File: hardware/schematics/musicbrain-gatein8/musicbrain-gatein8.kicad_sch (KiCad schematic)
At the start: 32 parts, among them J1 BUS, J2 GATES IN, U1 74HC165, U2 74LVC1G125

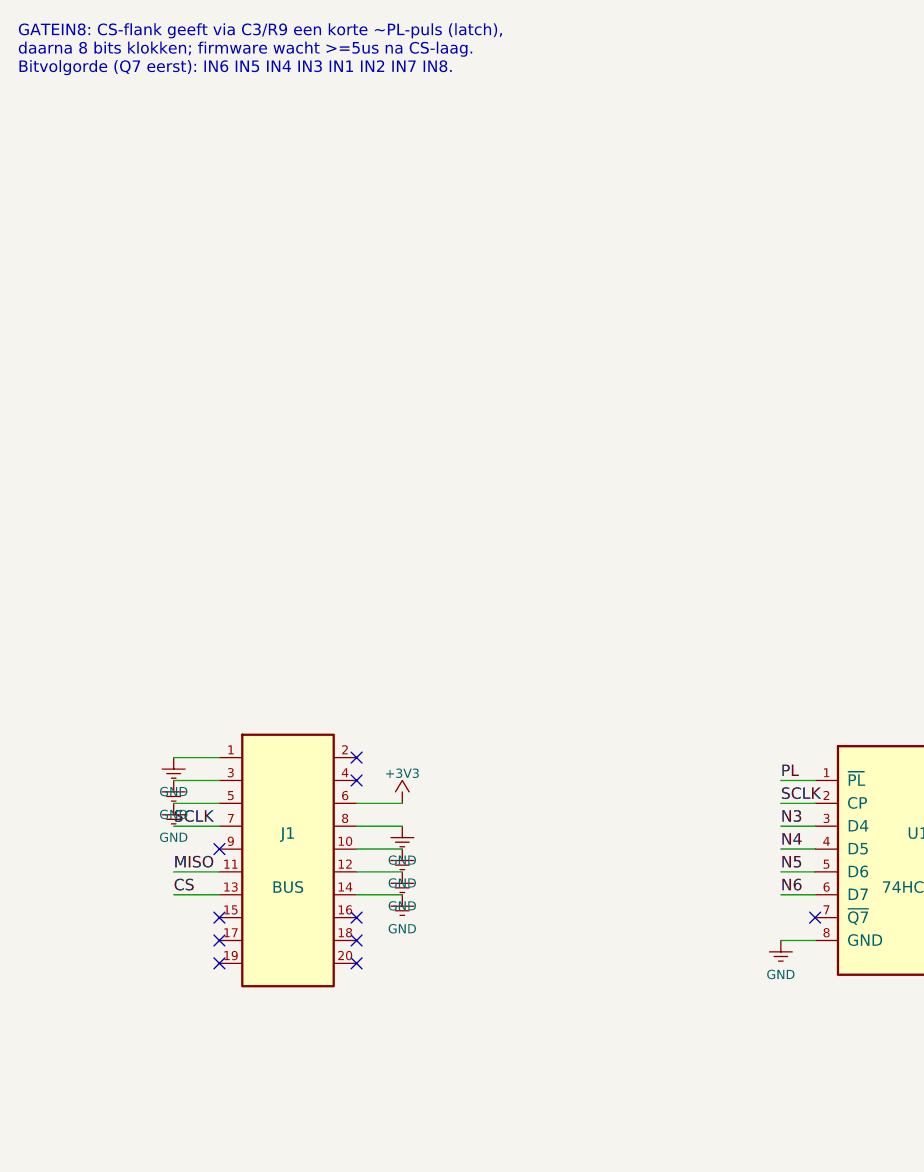
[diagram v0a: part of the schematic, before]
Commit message: gatein8 gen 2: 80x45, slot 2x12, freerouting
- kaart 40x80 -> 80x45 (bus.KAART_B x bus.H); J1 2x10 -> 2x12 via bus.j1_map
- J2 1x10 gecentreerd op het kaarthart, paneelinzet 4,04
- kanaal-conditionering (100k/100k/BAT54S) in kolommen onder de J2-pinnen;
  D_OF_IN-mapping ongewijzigd (firmware-contract)
- handroutes vervangen door freerouting-SES + gnd_stitch.json
- ERC 0, netcheck OK, DRC 0/0

Co-Authored-By: Claude Fable 5 <noreply@anthropic.com>
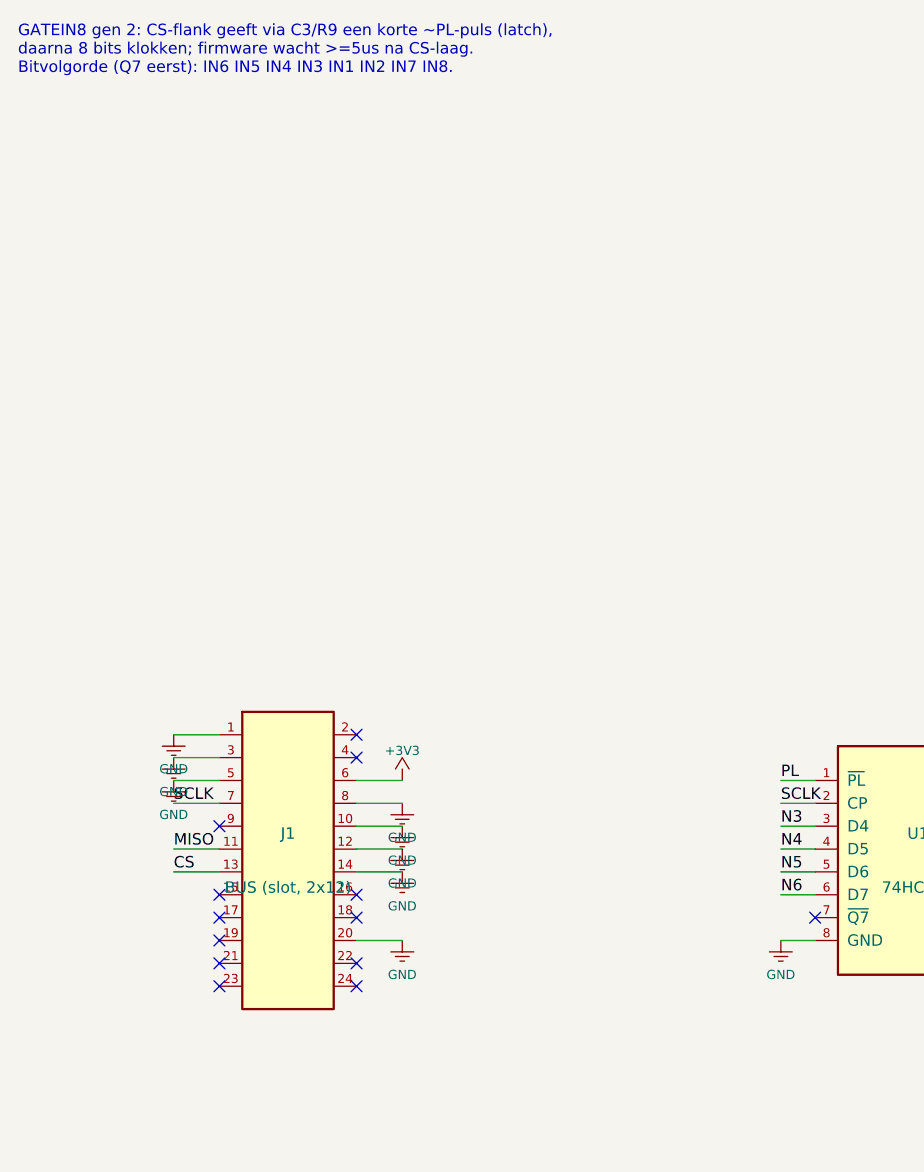
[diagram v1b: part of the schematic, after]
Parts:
- removed C1: 100n, Capacitor_SMD:C_0805_2012Metric, symbol Device:C
- removed R1, R2, R3, R4, R5, R6, R7, R8: 100k, Resistor_SMD:R_0805_2012Metric, symbol Device:R
- removed R9: 10k, Resistor_SMD:R_0805_2012Metric, symbol Device:R
- added C2: 10u, Capacitor_SMD:CP_Elec_4x5.3, symbol Device:C_Polarized
- added C3: 220p, Capacitor_SMD:C_0805_2012Metric, symbol Device:C
- added D1, D2, D3, D4, D5, D6, D7, D8: BAT54S, Package_TO_SOT_SMD:SOT-23, symbol Custom:BAT54S
- C1: renamed from C2; value 10u -> 100n; footprint Capacitor_SMD:CP_Elec_4x5.3 -> Capacitor_SMD:C_0805_2012Metric; symbol Device:C_Polarized -> Device:C
- J1: value BUS -> BUS (slot, 2x12); footprint Connector_PinHeader_2.54mm:PinHeader_2x10_P2.54mm_Horizontal -> Connector_PinHeader_2.54mm:PinHeader_2x12_P2.54mm_Horizontal; symbol Custom:Conn_02x10 -> Custom:Conn_02x12
- R11: renamed from D1; value BAT54S -> 100k; footprint Package_TO_SOT_SMD:SOT-23 -> Resistor_SMD:R_0805_2012Metric; symbol Custom:BAT54S -> Device:R
- R12: renamed from D2; value BAT54S -> 100k; footprint Package_TO_SOT_SMD:SOT-23 -> Resistor_SMD:R_0805_2012Metric; symbol Custom:BAT54S -> Device:R
- R13: renamed from D3; value BAT54S -> 100k; footprint Package_TO_SOT_SMD:SOT-23 -> Resistor_SMD:R_0805_2012Metric; symbol Custom:BAT54S -> Device:R
- R14: renamed from D4; value BAT54S -> 100k; footprint Package_TO_SOT_SMD:SOT-23 -> Resistor_SMD:R_0805_2012Metric; symbol Custom:BAT54S -> Device:R
- R15: renamed from D5; value BAT54S -> 100k; footprint Package_TO_SOT_SMD:SOT-23 -> Resistor_SMD:R_0805_2012Metric; symbol Custom:BAT54S -> Device:R
- R16: renamed from D6; value BAT54S -> 100k; footprint Package_TO_SOT_SMD:SOT-23 -> Resistor_SMD:R_0805_2012Metric; symbol Custom:BAT54S -> Device:R
- R17: renamed from D7; value BAT54S -> 100k; footprint Package_TO_SOT_SMD:SOT-23 -> Resistor_SMD:R_0805_2012Metric; symbol Custom:BAT54S -> Device:R
- R18: renamed from D8; value BAT54S -> 100k; footprint Package_TO_SOT_SMD:SOT-23 -> Resistor_SMD:R_0805_2012Metric; symbol Custom:BAT54S -> Device:R
- R9: renamed from C3; value 220p -> 10k; footprint Capacitor_SMD:C_0805_2012Metric -> Resistor_SMD:R_0805_2012Metric; symbol Device:C -> Device:R
- renumbered R11 to R1, R12 to R2, R13 to R3, R14 to R4, R15 to R5, R16 to R6, R17 to R7, R18 to R8
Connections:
- net +3V3: now also R9.1, C2.1 (+), D1.2 (K2), D2.2 (K2), D3.2 (K2), D4.2 (K2), D5.2 (K2), D6.2 (K2), D7.2 (K2), D8.2 (K2); no longer R11.2 (K2), R12.2 (K2), R13.2 (K2), R14.2 (K2), R15.2 (K2), R16.2 (K2), R17.2 (K2), R18.2 (K2)
- net CS: now also C3.2; no longer R9.2
- net GND: now also J1.20 (Pin_20), R11.2, R12.2, R13.2, R14.2, R15.2, R16.2, R17.2, R18.2, C2.2 (-), D1.1 (A1), D2.1 (A1), D3.1 (A1), D4.1 (A1), D5.1 (A1), D6.1 (A1), D7.1 (A1), D8.1 (A1); no longer R1.2, R11.1 (A1), R12.1 (A1), R13.1 (A1), R14.1 (A1), R15.1 (A1), R16.1 (A1), R17.1 (A1), R18.1 (A1), R2.2, R3.2, R4.2, R5.2, R6.2, R7.2, R8.2
- net IN1: now also R1.1
- net IN2: now also R2.1
- net IN3: now also R3.1
- net IN4: now also R4.1
- net IN5: now also R5.1
- net IN6: now also R6.1
- net IN7: now also R7.1
- net IN8: now also R8.1
- net N1: now also R1.2, R11.1, D1.3 (K1A2); no longer R1.1, R11.3 (K1A2)
- net N2: now also R12.1, R2.2, D2.3 (K1A2); no longer R12.3 (K1A2), R2.1
- net N3: now also R13.1, R3.2, D3.3 (K1A2); no longer R13.3 (K1A2), R3.1
- net N4: now also R14.1, R4.2, D4.3 (K1A2); no longer R14.3 (K1A2), R4.1
- net N5: now also R15.1, R5.2, D5.3 (K1A2); no longer R15.3 (K1A2), R5.1
- net N6: now also R16.1, R6.2, D6.3 (K1A2); no longer R16.3 (K1A2), R6.1
- net N7: now also R17.1, R7.2, D7.3 (K1A2); no longer R17.3 (K1A2), R7.1
- net N8: now also R18.1, R8.2, D8.3 (K1A2); no longer R18.3 (K1A2), R8.1
- net PL: now also R9.2, C3.1; no longer R9.1
- no-connect marks 10 -> 13
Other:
- note added: "GATEIN8 gen 2: CS-flank geeft via C3/R9 een korte ~PL-puls (latch), daarna 8 bits klokken; firmware wacht >=5us na CS-laag. Bitvolgorde (Q7 eerst): IN6 IN5 IN4 IN3 IN1 IN2 IN7 IN8."
- note removed: "GATEIN8: CS-flank geeft via C3/R9 een korte ~PL-puls (latch), daarna 8 bits klokken; firmware wacht >=5us na CS-laag. Bitvolgorde (Q7 eerst): IN6 IN5 IN4 IN3 IN1 IN2 IN7 IN8."
- moved on the sheet: R1, R2, R3, R4, R5, R6, R7, R8
